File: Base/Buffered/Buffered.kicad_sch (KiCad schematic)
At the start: 24 parts, among them J1 Conn_01x04_Pin, J2 Conn_01x04_Pin, J3 AudioJack2_Ground, J4 AudioJack2_Ground, J5 Barrel_Jack_Switch, Q1 40V, Q2 DMC3071LVT

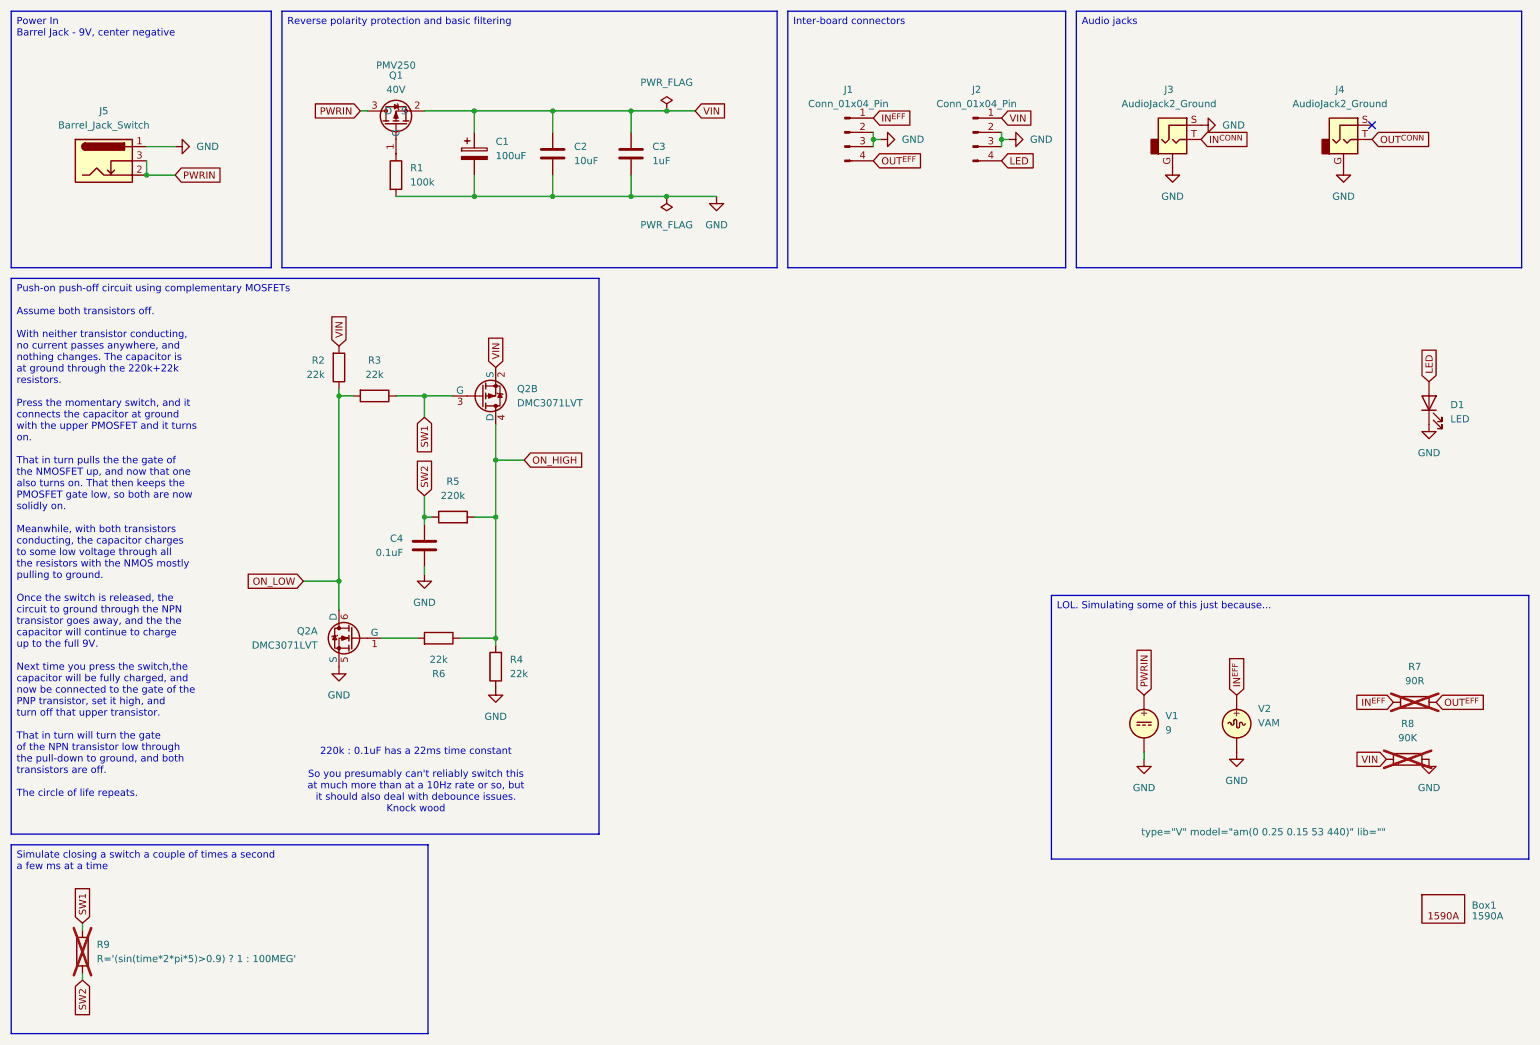
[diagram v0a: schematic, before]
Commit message: Wire the soft-switch up to actually switch signal and LED
Surprisingly, this actually seems to work fine.  In simulation only, of
course.

And not surprisingly, according to the same simulation, it has an
impressively horrible pop at switching time.  This very much reminds me
of the broken "Tremolo doubling as a metronome" thing, which was due to
the exact same thing: very harsh and sudden driving of the JFET gate.

It's made worse by the MOSFET switching having the same thing.  Big
voltage spike when turning off, presumably due to capacitive parasitics
or whatever.

Possibly helped by adding a resistor at the gate or something, but
unlike the tremolo, the switching event is rare.  So right now I simply
don't care.  I'm just _simulating_ switching things at a 5Hz rate, so it
shows up like a sore thumb.

I haven't done layout, and I haven't added a real switch yet, so this is
all just simulation.

Signed-off-by: Linus Torvalds <torvalds@linux-foundation.org>
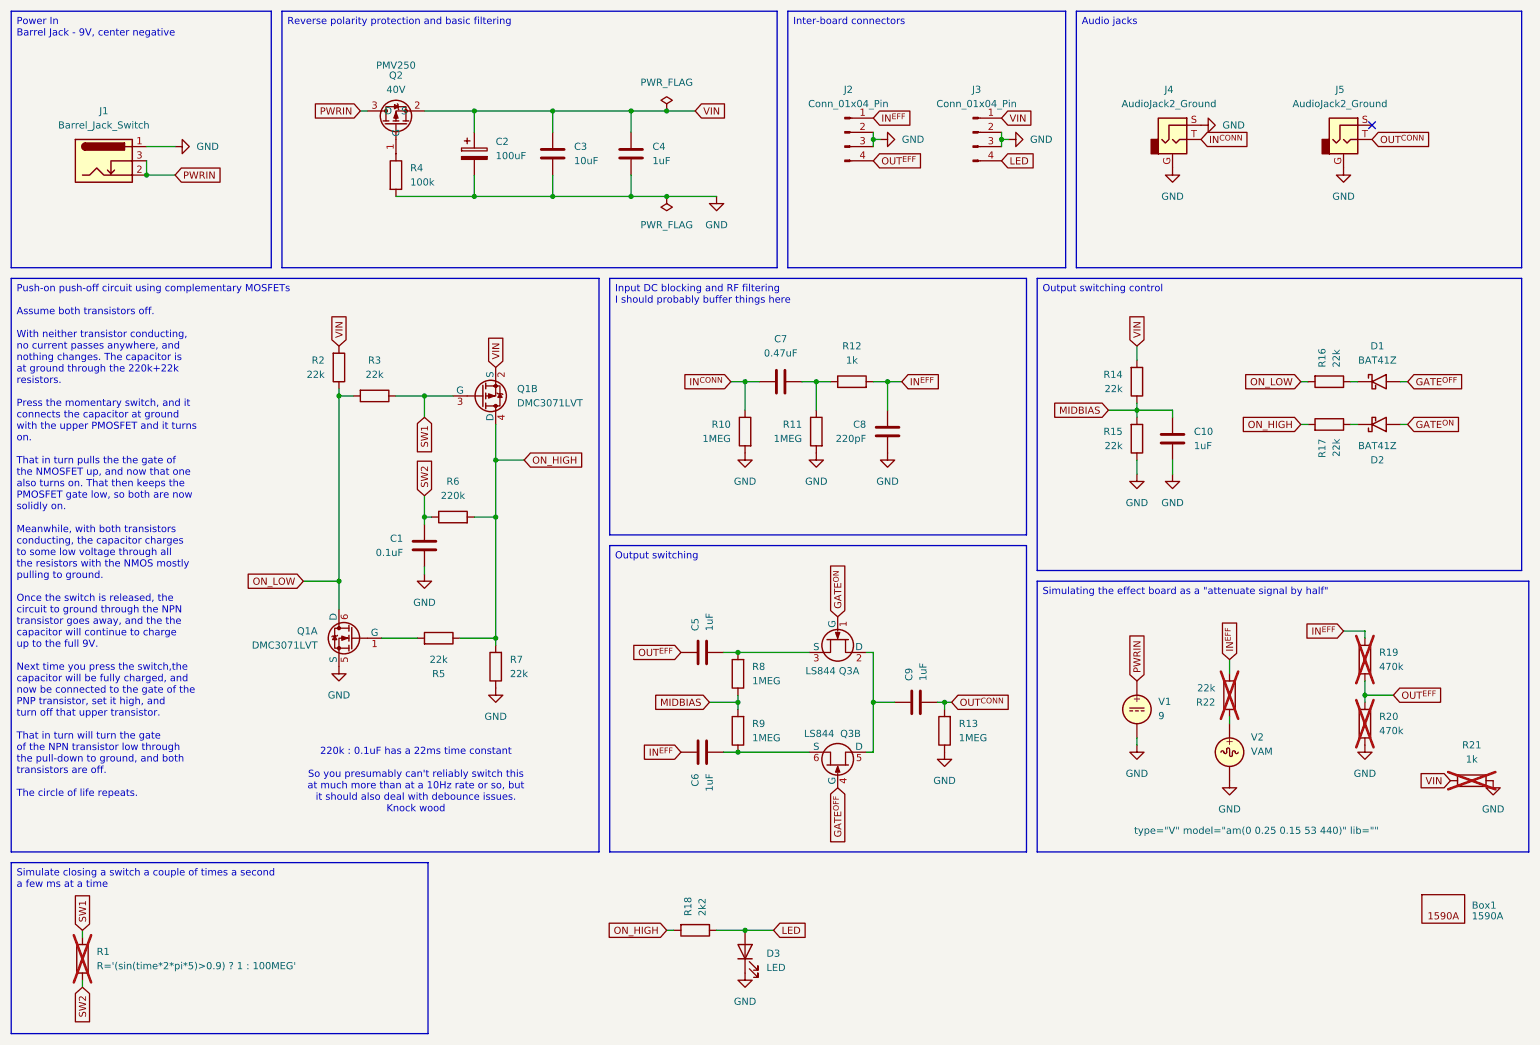
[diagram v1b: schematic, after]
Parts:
- added C10, C5, C6, C9: 1uF, Capacitor_SMD:C_1206_3216Metric, symbol Device:C
- added C7: 0.47uF, Capacitor_SMD:C_1206_3216Metric, symbol Device:C
- added C8: 220pF, Capacitor_SMD:C_0805_2012Metric, symbol Device:C
- added D1, D2: BAT41Z, Diode_SMD:D_SOD-123, symbol Mylib:BAT41ZFILM
- added Q3: LS844, Package_TO_SOT_SMD:SOT-23-6, symbol Mylib:LS844
- added R10, R11, R13, R8, R9: 1MEG, Resistor_SMD:R_0805_2012Metric, symbol Device:R
- added R12: 1k, Resistor_SMD:R_0805_2012Metric, symbol Device:R
- added R14, R15, R16, R17, R22: 22k, Resistor_SMD:R_0805_2012Metric, symbol Device:R
- added R18: 2k2, Resistor_SMD:R_0805_2012Metric, symbol Device:R
- added R20: 470k, symbol Device:R
- R19: renamed from R7; value 90R -> 470k
- R21: renamed from R8; value 90K -> 1k
- renumbered C4 to C1, C1 to C2, C2 to C3, C3 to C4, D1 to D3, J5 to J1, J1 to J2, J2 to J3, J3 to J4, J4 to J5, Q2 to Q1, Q1 to Q2, R9 to R1, R1 to R4, R6 to R5, R5 to R6, R4 to R7
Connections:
- net GND: now also C10.2, C8.2, R10.2, R11.2, R13.1, R15.1, R20.1
- net IN^{CONN}: now also C7.1, R10.1
- net IN^{EFF}: now also R19.2, C6.1, C8.1, R12.2, R22.1; no longer R19.1, V2.1
- net LED: now also R18.1
- net ON_HIGH: now also R17.2, R18.2
- net ON_LOW: now also R16.2
- net OUT^{CONN}: now also C9.2, R13.2
- net OUT^{EFF}: now also R19.1, C5.1, R20.2; no longer R19.2
- net VIN: now also R14.2
- new net: D2.1 (K), R17.1
- new net: D1.1 (K), R16.1
- new net: C5.2, Q3.3 (S), R8.2
- new net: R22.2, V2.1
- new net: C7.2, R11.1, R12.1
- new net: C6.2, Q3.6 (S), R9.1
- new net: C9.1, Q3.2 (D), Q3.5 (D)
- new net GATE^{OFF}: D1.2 (A), Q3.4 (G)
- new net GATE^{ON}: D2.2 (A), Q3.1 (G)
- new net MIDBIAS: C10.1, R14.1, R15.2, R8.1, R9.2
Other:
- moved on the sheet: D3, R1, R19, R21, V1, V2

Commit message: Buffered base: add RF filter after JFET switches
It turns out that getting rid of the switching pop seems to be as simple
as that.

Maybe time to do PCB layout and see if reality matches simulation?

I do think I should do the buffer that this doesn't do despite the name.
That was the intent, but then it worked so well without it..  An op-amp
would be the sane thing to do, but since I've been on a "discrete
components" tear, I suspect I'd just do a JFET voltage follower.

But then I feel like I should make up for the inevitable signal loss.
Or use a common source thing that does a phase reversal? That seems
wrong too.  Perhaps do another dual JFET for a common source both at
input and output?

Decisions, decisions.

Anyway, this doesn't do any of that.  This just gets rid of the
switching pop in simulation.

Signed-off-by: Linus Torvalds <torvalds@linux-foundation.org>
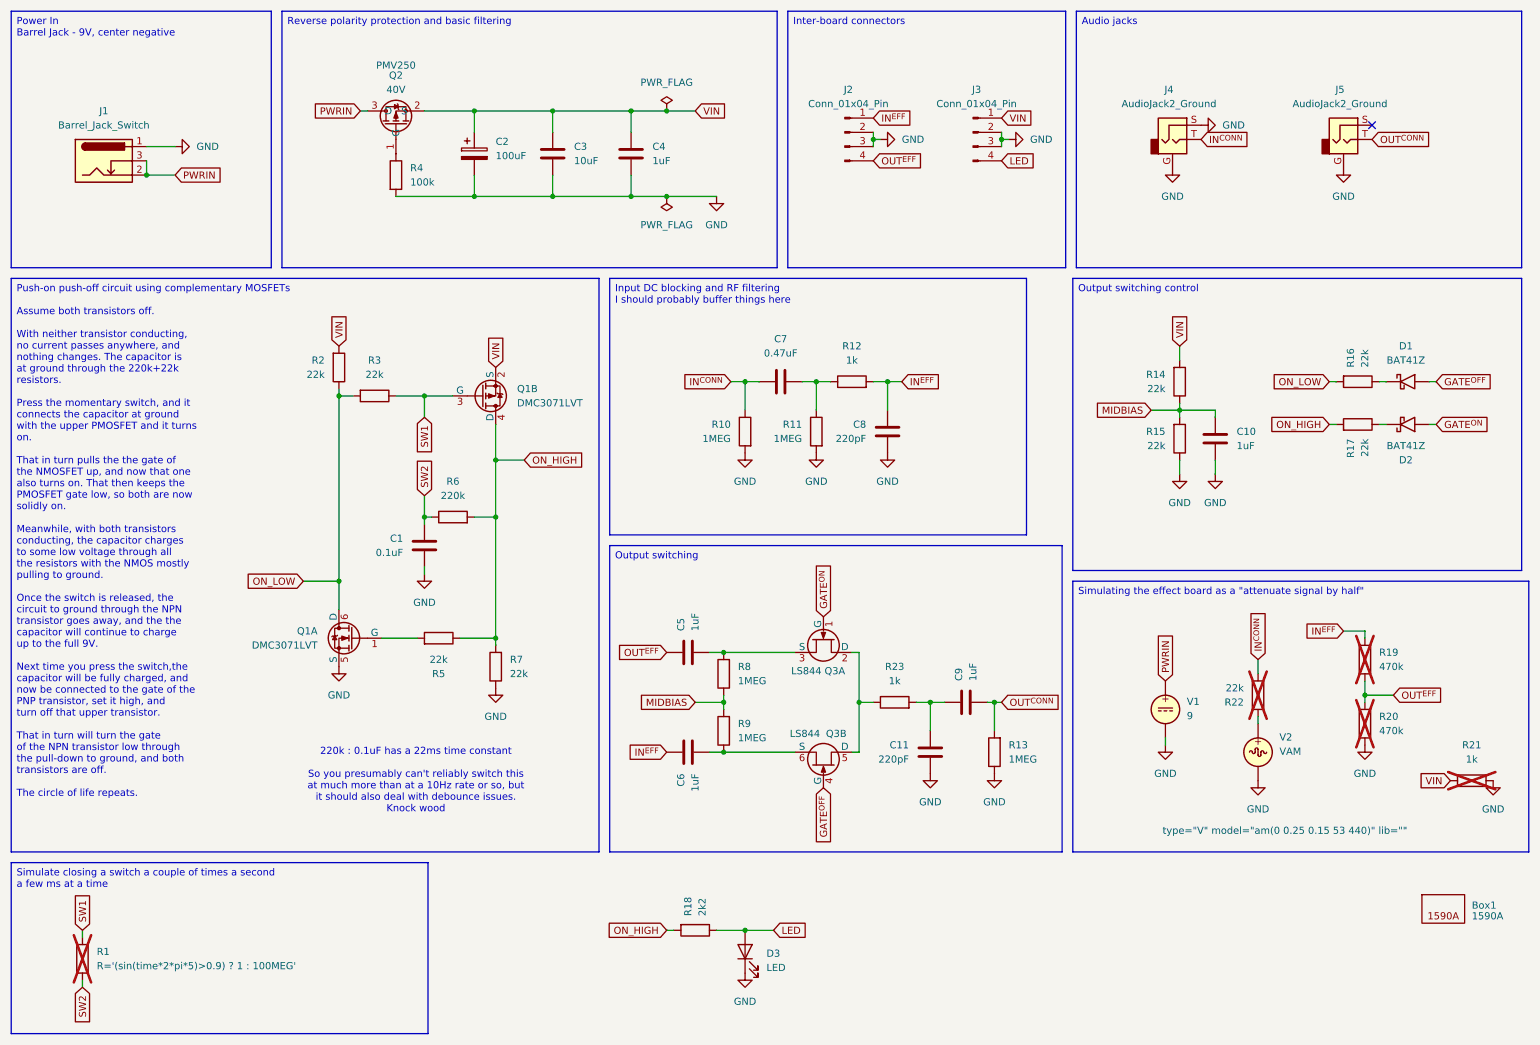
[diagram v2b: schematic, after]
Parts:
- added C11: 220pF, Capacitor_SMD:C_0805_2012Metric, symbol Device:C
- added R23: 1k, Resistor_SMD:R_0805_2012Metric, symbol Device:R
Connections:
- net GND: now also C11.2
- net IN^{CONN}: now also R22.1
- net IN^{EFF}: no longer R22.1
- net at Q3.2 (D), Q3.5 (D): now also R23.1; no longer C9.1
- new net: C11.1, C9.1, R23.2
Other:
- moved on the sheet: C10, C5, C6, C9, D1, D2, Q3A, Q3B, R13, R14, R15, R16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

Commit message: Split the buffered base over multiple schematic pages, do PCB layout
So this thing is still mis-named, in that it doesn't actually buffer the
signal at all, it only does the transistor soft-switching.  But I _will_
add buffering at some point, it's just not the interesting part of this
all, since I've done that part before.

But because I wrote explanations for the push-on / push-off circuit, and
because I split things up into small parts, the schematic was getting
pretty crowded.  So I decided to split up the actually interesting part
of the schematic - the switching side - onto a schematic page of its
own.

And while doing that, I moved the simulation infrastructure to its own
page too.

That leaves the toplevel page pretty empty with mainly just the
connectors and the basic signal and power filtering, but that's where
the buffers will go eventually.

And because it simulates fine, I want to actually see if it works in
reality.  So this also does the PCB layout.  There's tons of room left
for any future buffering circuit, whether I then do it with discrete
JFETs or decide that op-amps are the sane thing here.

I used a random regular tactile switch - which I don't actually have in
my parts library.  I'll just wire up two wires and test it that way (and
I do have some momentary SPDT stomp switches around that I can attach to
the wires).

But longer-term, one of the points of this kind of electronic switching
is that you can do it multiple ways, and aren't limited to a physical
switch - or indeed just a single one.  So maybe I'll do some remote
switching thing, or play around with using a hall effect sensor and a
magnet, or whatever.

There are always new things to learn about...  But let's make sure the
basics of this thing actually works first.

Signed-off-by: Linus Torvalds <torvalds@linux-foundation.org>
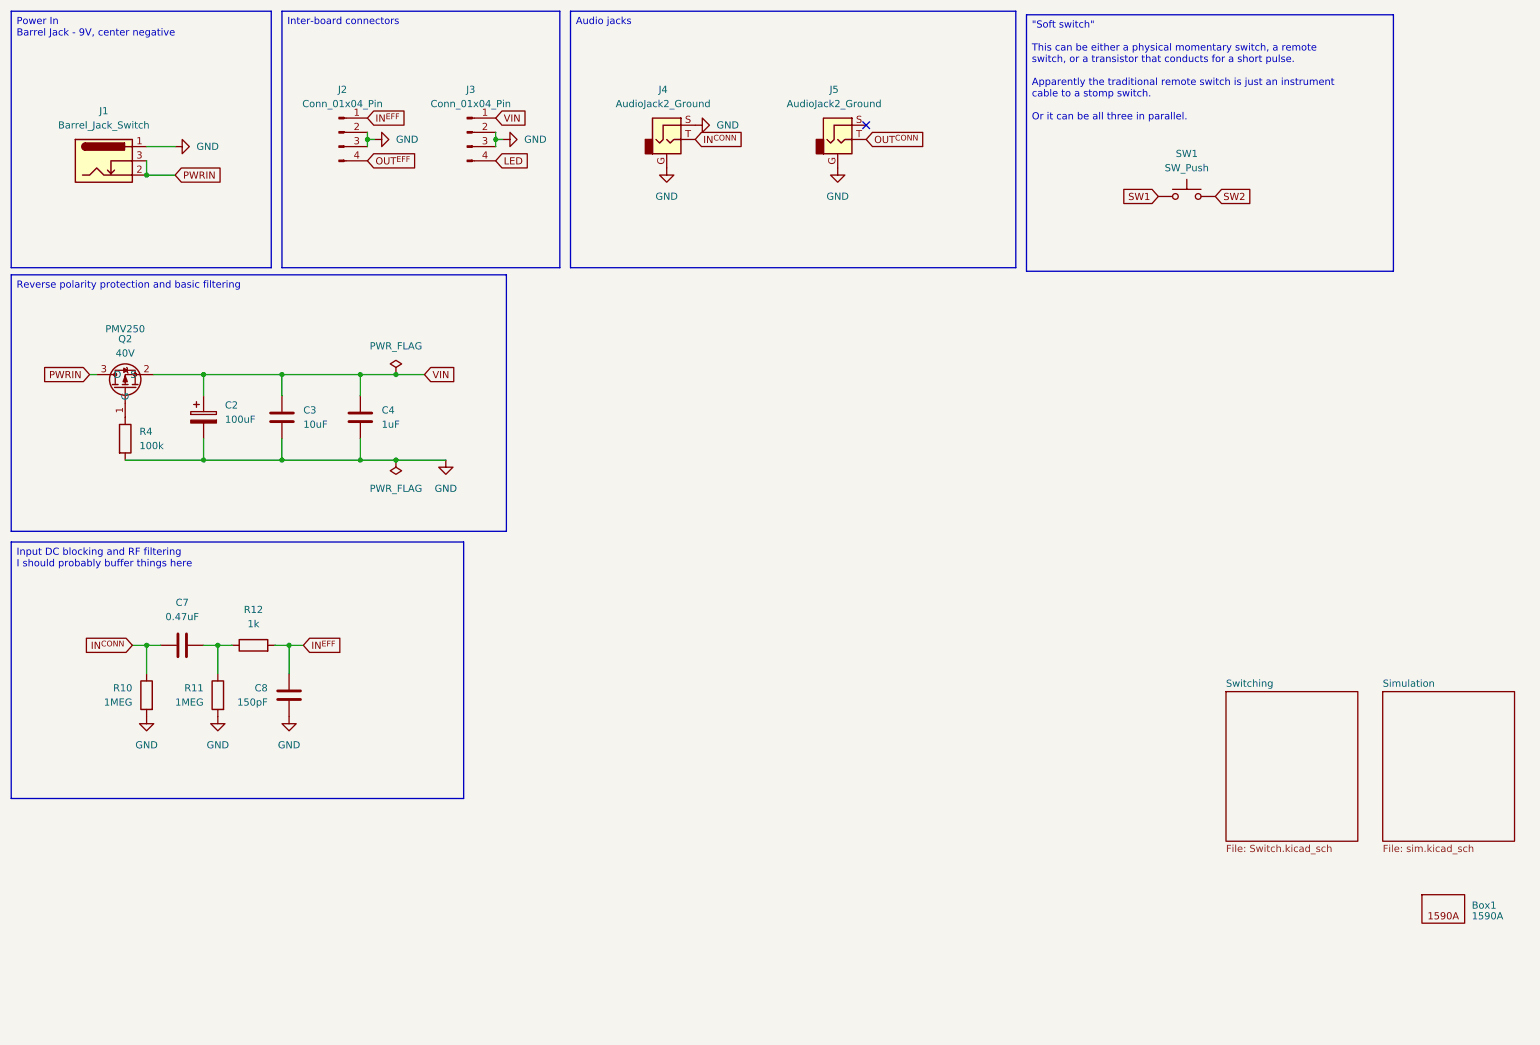
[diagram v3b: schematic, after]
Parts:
- removed C1: 0.1uF, Mylib:C_0704_1810Metric, symbol Device:C
- removed C10, C5, C6, C9: 1uF, Capacitor_SMD:C_1206_3216Metric, symbol Device:C
- removed C11: 220pF, Capacitor_SMD:C_0805_2012Metric, symbol Device:C
- removed D1, D2: BAT41Z, Diode_SMD:D_SOD-123, symbol Mylib:BAT41ZFILM
- removed D3: LED, LED_THT:LED_D5.0mm, symbol Device:LED
- removed Q1: DMC3071LVT, Package_TO_SOT_SMD:TSOT-23-6, symbol Mylib:DMC3071LVT
- removed Q3: LS844, Package_TO_SOT_SMD:SOT-23-6, symbol Mylib:LS844
- removed R1: R='(sin(time*2*pi*5)>0.9) ? 1 : 100MEG', Resistor_SMD:R_0805_2012Metric, symbol Device:R
- removed R13, R8, R9: 1MEG, Resistor_SMD:R_0805_2012Metric, symbol Device:R
- removed R14, R15, R16, R17, R2, R22, R3, R5, R7: 22k, Resistor_SMD:R_0805_2012Metric, symbol Device:R
- removed R18: 2k2, Resistor_SMD:R_0805_2012Metric, symbol Device:R
- removed R19, R20: 470k, symbol Device:R
- removed R21: 1k, symbol Device:R
- removed R23: 1k, Resistor_SMD:R_0805_2012Metric, symbol Device:R
- removed R6: 220k, Resistor_SMD:R_0805_2012Metric, symbol Device:R
- removed V1: 9, symbol Simulation_SPICE:VDC
- removed V2: VAM, symbol Simulation_SPICE:VAM
- added SW1: SW_Push, Button_Switch_THT:SW_PUSH_6mm, symbol Switch:SW_Push
- C8: value 220pF -> 150pF
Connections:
- net SW1: now also SW1.1
- net SW2: now also SW1.2
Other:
- added sheet Simulation (sim.kicad_sch)
- added sheet Switching (Switch.kicad_sch)
- note removed: "220k : 0.1uF has a 22ms time constant So you presumably can't reliably switch this at much more than at a 10Hz rate or so, but it should also deal with debounce issues. Knock wood"
- title: Plain Passive Base Board -> Buffered Base Board
- moved on the sheet: C2, C3, C4, C7, C8, J2, J3, J4, J5, Q2, R10, R11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
